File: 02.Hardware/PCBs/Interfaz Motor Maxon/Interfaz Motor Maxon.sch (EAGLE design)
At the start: 4 parts, among them J1 1-84953-1, J2 52207-1133

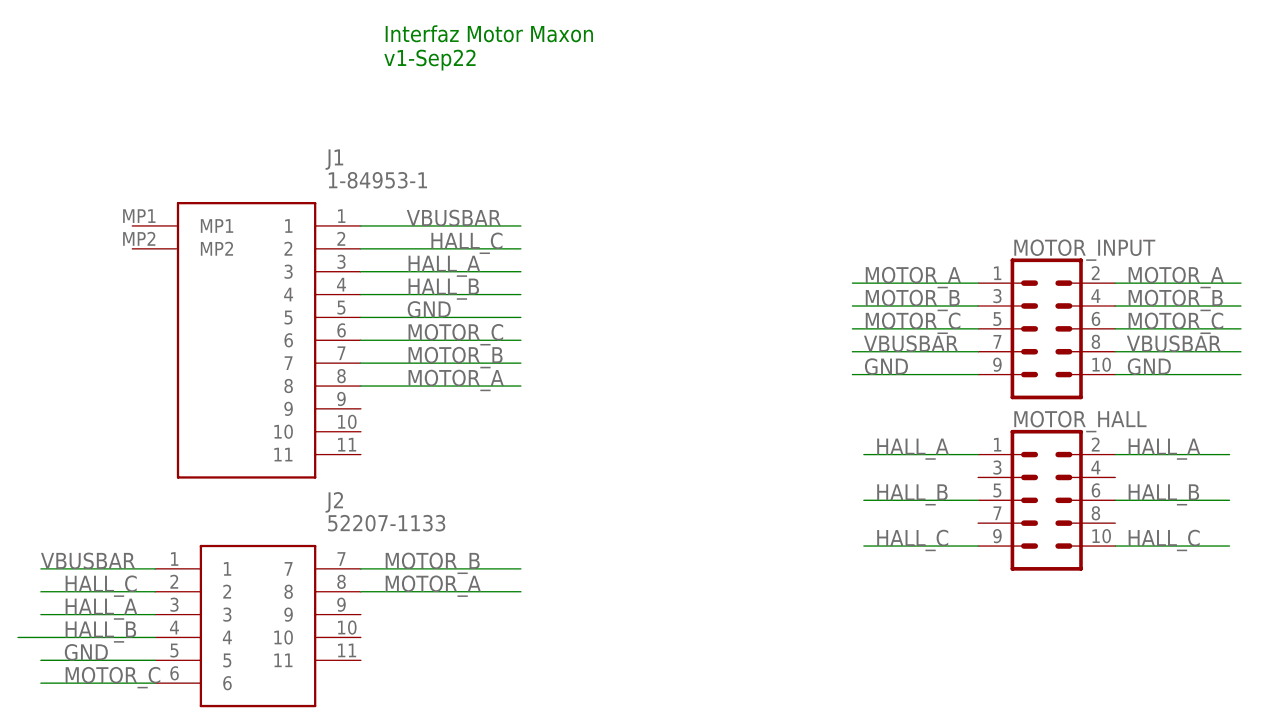
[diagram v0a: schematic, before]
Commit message: Correcion errores. Interfaz Maxon v2
Correcion de conexiones entre los conectores del motores y los conectores a la placa.
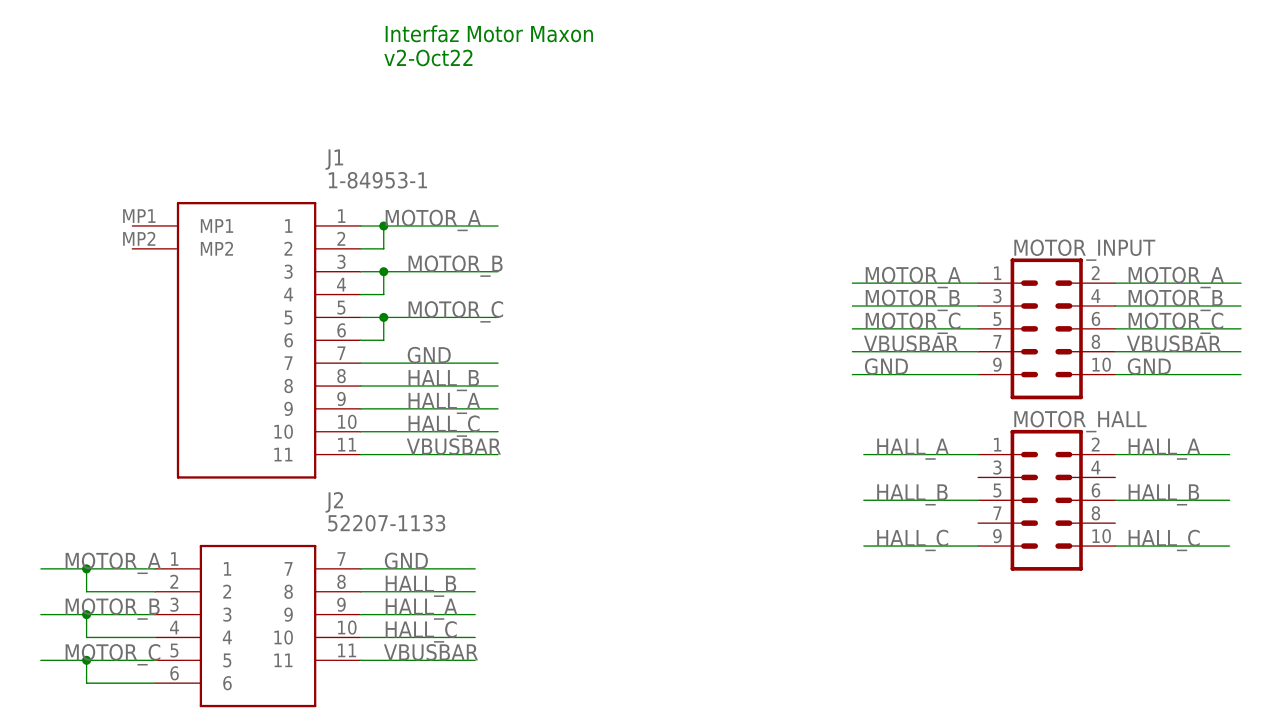
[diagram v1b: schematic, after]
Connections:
- net GND: now also J1.7, J2.7; no longer J1.5, J2.5
- net HALL_A: now also J1.9, J2.9; no longer J1.3, J2.3
- net HALL_B: now also J1.8, J2.8; no longer J1.4, J2.4
- net HALL_C: now also J1.10, J2.10; no longer J1.2, J2.2
- net MOTOR_A: now also J1.1, J1.2, J2.1, J2.2; no longer J1.8, J2.8
- net MOTOR_B: now also J1.3, J1.4, J2.3, J2.4; no longer J1.7, J2.7
- net MOTOR_C: now also J1.5, J2.5
- net VBUSBAR: now also J1.11, J2.11; no longer J1.1, J2.1
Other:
- note added: "Interfaz Motor Maxon v2-Oct22"
- note removed: "Interfaz Motor Maxon v1-Sep22"
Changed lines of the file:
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@@
 <plain>
 <text x="45.72" y="78.74" size="1.778" layer="91">Interfaz Motor Maxon
-v1-Sep22</text>
+v2-Oct22</text>
 </plain>
 <instances>
@@
 <net name="HALL_C" class="0">
 <segment>
-<pinref part="J1" gate="G$1" pin="2"/>
-<wire x1="43.18" y1="58.42" x2="60.96" y2="58.42" width="0.1524" layer="91"/>
-<label x="50.8" y="58.42" size="1.778" layer="95"/>
-</segment>
-<segment>
-<pinref part="J2" gate="G$1" pin="2"/>
-<wire x1="20.32" y1="20.32" x2="7.62" y2="20.32" width="0.1524" layer="91"/>
-<label x="10.16" y="20.32" size="1.778" layer="95"/>
-</segment>
-<segment>
 <pinref part="MOTOR_HALL" gate="G$1" pin="9"/>
 <wire x1="111.76" y1="25.4" x2="99.06" y2="25.4" width="0.1524" layer="91"/>
@@
 <pinref part="MOTOR_HALL" gate="G$1" pin="10"/>
 </segment>
+<segment>
+<pinref part="J2" gate="G$1" pin="10"/>
+<wire x1="43.18" y1="15.24" x2="55.88" y2="15.24" width="0.1524" layer="91"/>
+<label x="45.72" y="15.24" size="1.778" layer="95"/>
+</segment>
+<segment>
+<pinref part="J1" gate="G$1" pin="10"/>
+<wire x1="43.18" y1="38.1" x2="58.42" y2="38.1" width="0.1524" layer="91"/>
+<label x="48.26" y="38.1" size="1.778" layer="95"/>
+</segment>
 </net>
 <net name="HALL_A" class="0">
-<segment>
-<pinref part="J1" gate="G$1" pin="3"/>
-<wire x1="43.18" y1="55.88" x2="60.96" y2="55.88" width="0.1524" layer="91"/>
-<label x="48.26" y="55.88" size="1.778" layer="95"/>
-</segment>
-<segment>
-<pinref part="J2" gate="G$1" pin="3"/>
-<wire x1="20.32" y1="17.78" x2="7.62" y2="17.78" width="0.1524" layer="91"/>
-<label x="10.16" y="17.78" size="1.778" layer="95"/>
-</segment>
 <segment>
 <pinref part="MOTOR_HALL" gate="G$1" pin="1"/>
@@
 <pinref part="MOTOR_HALL" gate="G$1" pin="2"/>
 </segment>
+<segment>
+<pinref part="J1" gate="G$1" pin="9"/>
+<wire x1="43.18" y1="40.64" x2="58.42" y2="40.64" width="0.1524" layer="91"/>
+<label x="48.26" y="40.64" size="1.778" layer="95"/>
+</segment>
+<segment>
+<pinref part="J2" gate="G$1" pin="9"/>
+<wire x1="43.18" y1="17.78" x2="55.88" y2="17.78" width="0.1524" layer="91"/>
+<label x="45.72" y="17.78" size="1.778" layer="95"/>
+</segment>
 </net>
 <net name="HALL_B" class="0">
-<segment>
-<pinref part="J1" gate="G$1" pin="4"/>
-<wire x1="43.18" y1="53.34" x2="60.96" y2="53.34" width="0.1524" layer="91"/>
-<label x="48.26" y="53.34" size="1.778" layer="95"/>
-</segment>
-<segment>
-<pinref part="J2" gate="G$1" pin="4"/>
-<wire x1="20.32" y1="15.24" x2="5.08" y2="15.24" width="0.1524" layer="91"/>
-<label x="10.16" y="15.24" size="1.778" layer="95"/>
-</segment>
 <segment>
 <pinref part="MOTOR_HALL" gate="G$1" pin="5"/>
@@
 <pinref part="MOTOR_HALL" gate="G$1" pin="6"/>
 </segment>
+<segment>
+<pinref part="J1" gate="G$1" pin="8"/>
+<wire x1="43.18" y1="43.18" x2="58.42" y2="43.18" width="0.1524" layer="91"/>
+<label x="48.26" y="43.18" size="1.778" layer="95"/>
+</segment>
+<segment>
+<pinref part="J2" gate="G$1" pin="8"/>
+<wire x1="43.18" y1="20.32" x2="55.88" y2="20.32" width="0.1524" layer="91"/>
+<label x="45.72" y="20.32" size="1.778" layer="95"/>
+</segment>
 </net>
 <net name="GND" class="0">
-<segment>
-<pinref part="J1" gate="G$1" pin="5"/>
-<wire x1="43.18" y1="50.8" x2="60.96" y2="50.8" width="0.1524" layer="91"/>
-<label x="48.26" y="50.8" size="1.778" layer="95"/>
-</segment>
-<segment>
-<pinref part="J2" gate="G$1" pin="5"/>
-<wire x1="20.32" y1="12.7" x2="7.62" y2="12.7" width="0.1524" layer="91"/>
-<label x="10.16" y="12.7" size="1.778" layer="95"/>
-</segment>
 <segment>
 <pinref part="MOTOR_INPUT" gate="G$1" pin="9"/>
@@
 <pinref part="MOTOR_INPUT" gate="G$1" pin="10"/>
 </segment>
+<segment>
+<pinref part="J1" gate="G$1" pin="7"/>
+<wire x1="43.18" y1="45.72" x2="58.42" y2="45.72" width="0.1524" layer="91"/>
+<label x="48.26" y="45.72" size="1.778" layer="95"/>
+</segment>
+<segment>
+<pinref part="J2" gate="G$1" pin="7"/>
+<wire x1="43.18" y1="22.86" x2="55.88" y2="22.86" width="0.1524" layer="91"/>
+<label x="45.72" y="22.86" size="1.778" layer="95"/>
+</segment>
 </net>
 <net name="MOTOR_C" class="0">
-<segment>
-<pinref part="J2" gate="G$1" pin="6"/>
-<wire x1="20.32" y1="10.16" x2="7.62" y2="10.16" width="0.1524" layer="91"/>
-<label x="10.16" y="10.16" size="1.778" layer="95"/>
-</segment>
-<segment>
-<pinref part="J1" gate="G$1" pin="6"/>
-<wire x1="43.18" y1="48.26" x2="60.96" y2="48.26" width="0.1524" layer="91"/>
-<label x="48.26" y="48.26" size="1.778" layer="95"/>
-</segment>
 <segment>
 <pinref part="MOTOR_INPUT" gate="G$1" pin="5"/>
@@
 <pinref part="MOTOR_INPUT" gate="G$1" pin="6"/>
 </segment>
+<segment>
+<pinref part="J2" gate="G$1" pin="5"/>
+<wire x1="20.32" y1="12.7" x2="12.7" y2="12.7" width="0.1524" layer="91"/>
+<pinref part="J2" gate="G$1" pin="6"/>
+<wire x1="12.7" y1="12.7" x2="7.62" y2="12.7" width="0.1524" layer="91"/>
+<wire x1="20.32" y1="10.16" x2="12.7" y2="10.16" width="0.1524" layer="91"/>
+<wire x1="12.7" y1="10.16" x2="12.7" y2="12.7" width="0.1524" layer="91"/>
+<junction x="12.7" y="12.7"/>
+<label x="10.16" y="12.7" size="1.778" layer="95"/>
+</segment>
+<segment>
+<pinref part="J1" gate="G$1" pin="5"/>
+<wire x1="43.18" y1="50.8" x2="45.72" y2="50.8" width="0.1524" layer="91"/>
+<pinref part="J1" gate="G$1" pin="6"/>
+<wire x1="45.72" y1="50.8" x2="58.42" y2="50.8" width="0.1524" layer="91"/>
+<wire x1="43.18" y1="48.26" x2="45.72" y2="48.26" width="0.1524" layer="91"/>
+<wire x1="45.72" y1="48.26" x2="45.72" y2="50.8" width="0.1524" layer="91"/>
+<junction x="45.72" y="50.8"/>
+<label x="48.26" y="50.8" size="1.778" layer="95"/>
+</segment>
 </net>
 <net name="MOTOR_B" class="0">
-<segment>
-<pinref part="J2" gate="G$1" pin="7"/>
-<wire x1="43.18" y1="22.86" x2="60.96" y2="22.86" width="0.1524" layer="91"/>
-<label x="45.72" y="22.86" size="1.778" layer="95"/>
-</segment>
-<segment>
-<pinref part="J1" gate="G$1" pin="7"/>
-<wire x1="43.18" y1="45.72" x2="60.96" y2="45.72" width="0.1524" layer="91"/>
-<label x="48.26" y="45.72" size="1.778" layer="95"/>
-</segment>
 <segment>
 <pinref part="MOTOR_INPUT" gate="G$1" pin="3"/>
@@
 <pinref part="MOTOR_INPUT" gate="G$1" pin="4"/>
 </segment>
+<segment>
+<pinref part="J1" gate="G$1" pin="3"/>
+<wire x1="43.18" y1="55.88" x2="45.72" y2="55.88" width="0.1524" layer="91"/>
+<pinref part="J1" gate="G$1" pin="4"/>
+<wire x1="45.72" y1="55.88" x2="58.42" y2="55.88" width="0.1524" layer="91"/>
+<wire x1="43.18" y1="53.34" x2="45.72" y2="53.34" width="0.1524" layer="91"/>
+<wire x1="45.72" y1="53.34" x2="45.72" y2="55.88" width="0.1524" layer="91"/>
+<junction x="45.72" y="55.88"/>
+<label x="48.26" y="55.88" size="1.778" layer="95"/>
+</segment>
+<segment>
+<pinref part="J2" gate="G$1" pin="3"/>
+<wire x1="20.32" y1="17.78" x2="12.7" y2="17.78" width="0.1524" layer="91"/>
+<pinref part="J2" gate="G$1" pin="4"/>
+<wire x1="12.7" y1="17.78" x2="7.62" y2="17.78" width="0.1524" layer="91"/>
+<wire x1="20.32" y1="15.24" x2="12.7" y2="15.24" width="0.1524" layer="91"/>
+<wire x1="12.7" y1="15.24" x2="12.7" y2="17.78" width="0.1524" layer="91"/>
+<junction x="12.7" y="17.78"/>
+<label x="10.16" y="17.78" size="1.778" layer="95"/>
+</segment>
 </net>
 <net name="MOTOR_A" class="0">
-<segment>
-<pinref part="J2" gate="G$1" pin="8"/>
-<wire x1="43.18" y1="20.32" x2="60.96" y2="20.32" width="0.1524" layer="91"/>
-<label x="45.72" y="20.32" size="1.778" layer="95"/>
-</segment>
-<segment>
-<pinref part="J1" gate="G$1" pin="8"/>
-<wire x1="43.18" y1="43.18" x2="60.96" y2="43.18" width="0.1524" layer="91"/>
-<label x="48.26" y="43.18" size="1.778" layer="95"/>
-</segment>
 <segment>
 <pinref part="MOTOR_INPUT" gate="G$1" pin="1"/>
@@
 <pinref part="MOTOR_INPUT" gate="G$1" pin="2"/>
 </segment>
+<segment>
+<pinref part="J1" gate="G$1" pin="2"/>
+<pinref part="J1" gate="G$1" pin="1"/>
+<wire x1="43.18" y1="60.96" x2="45.72" y2="60.96" width="0.1524" layer="91"/>
+<wire x1="45.72" y1="60.96" x2="58.42" y2="60.96" width="0.1524" layer="91"/>
+<wire x1="43.18" y1="58.42" x2="45.72" y2="58.42" width="0.1524" layer="91"/>
+<wire x1="45.72" y1="58.42" x2="45.72" y2="60.96" width="0.1524" layer="91"/>
+<junction x="45.72" y="60.96"/>
+<label x="45.72" y="60.96" size="1.778" layer="95"/>
+</segment>
+<segment>
+<pinref part="J2" gate="G$1" pin="1"/>
+<wire x1="20.32" y1="22.86" x2="12.7" y2="22.86" width="0.1524" layer="91"/>
+<pinref part="J2" gate="G$1" pin="2"/>
+<wire x1="12.7" y1="22.86" x2="7.62" y2="22.86" width="0.1524" layer="91"/>
+<wire x1="20.32" y1="20.32" x2="12.7" y2="20.32" width="0.1524" layer="91"/>
+<wire x1="12.7" y1="20.32" x2="12.7" y2="22.86" width="0.1524" layer="91"/>
+<junction x="12.7" y="22.86"/>
+<label x="10.16" y="22.86" size="1.778" layer="95"/>
+</segment>
 </net>
 <net name="VBUSBAR" class="0">
@@
 </segment>
 <segment>
-<pinref part="J1" gate="G$1" pin="1"/>
-<wire x1="43.18" y1="60.96" x2="60.96" y2="60.96" width="0.1524" layer="91"/>
-<label x="48.26" y="60.96" size="1.778" layer="95"/>
-</segment>
-<segment>
-<pinref part="J2" gate="G$1" pin="1"/>
-<wire x1="20.32" y1="22.86" x2="7.62" y2="22.86" width="0.1524" layer="91"/>
-<label x="7.62" y="22.86" size="1.778" layer="95"/>
-</segment>
-</net>
+<pinref part="J2" gate="G$1" pin="11"/>
+<wire x1="43.18" y1="12.7" x2="55.88" y2="12.7" width="0.1524" layer="91"/>
+<label x="45.72" y="12.7" size="1.778" layer="95"/>
+</segment>
+<segment>
+<pinref part="J1" gate="G$1" pin="11"/>
+<wire x1="43.18" y1="35.56" x2="58.42" y2="35.56" width="0.1524" layer="91"/>
+<label x="48.26" y="35.56" size="1.778" layer="95"/>
+</segment>
+</net>
